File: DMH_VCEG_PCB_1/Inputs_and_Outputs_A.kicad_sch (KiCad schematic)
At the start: 28 parts, among them J1 TS_Jack_6.35mm_Sw, J10 TS_Jack_6.35mm_Sw, J2 TS_Jack_6.35mm_Sw, J200 IDC_02x08, J3 TS_Jack_6.35mm_Sw, J4 TS_Jack_6.35mm_Sw, J5 TS_Jack_6.35mm_Sw, J6 TS_Jack_6.35mm_Sw, J7 TS_Jack_6.35mm_Sw, J8 TS_Jack_6.35mm_Sw, J9 TS_Jack_6.35mm_Sw, U8 TL074, U9 TL074

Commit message: Reanotated schematic
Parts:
- renumbered R1 to R66, R3 to R67, R5 to R68, R6 to R69, R67 to R71, R66 to R72, RV5 to RV15, RV6 to RV16, RV7 to RV17, RV8 to RV18, RV1 to RV19, RV2 to RV20, RV3 to RV21, RV4 to RV22, U9 to U1, U8 to U9
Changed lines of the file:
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@@
 		(dnp no)
 		(fields_autoplaced yes)
-		(property "Reference" "R66"
+		(property "Reference" "R72"
 			(at 165.1 226.06 90)
 			(effects
@@
 			(project "DMH_VCEG_PCB_1"
 				(path "/58f4306d-5387-4983-bb08-41a2313fd315/ce3fef8b-9f1d-4178-b50b-4a046c030679"
-					(reference "R66")
+					(reference "R72")
 					(unit 1)
 				)
@@
 		(on_board yes)
 		(dnp no)
-		(property "Reference" "U9"
+		(property "Reference" "U1"
 			(at 107.95 139.7 0)
 			(effects
@@
 			(project "DMH_VCEG_PCB_1"
 				(path "/58f4306d-5387-4983-bb08-41a2313fd315/ce3fef8b-9f1d-4178-b50b-4a046c030679"
-					(reference "U9")
+					(reference "U1")
 					(unit 4)
 				)
@@
 		(dnp no)
 		(fields_autoplaced yes)
-		(property "Reference" "R6"
+		(property "Reference" "R69"
 			(at 88.9 120.65 90)
 			(effects
@@
 			(project "DMH_VCEG_PCB_1"
 				(path "/58f4306d-5387-4983-bb08-41a2313fd315/ce3fef8b-9f1d-4178-b50b-4a046c030679"
-					(reference "R6")
+					(reference "R69")
 					(unit 1)
 				)
@@
 		(dnp no)
 		(fields_autoplaced yes)
-		(property "Reference" "R5"
+		(property "Reference" "R68"
 			(at 88.9 88.9 90)
 			(effects
@@
 			(project "DMH_VCEG_PCB_1"
 				(path "/58f4306d-5387-4983-bb08-41a2313fd315/ce3fef8b-9f1d-4178-b50b-4a046c030679"
-					(reference "R5")
+					(reference "R68")
 					(unit 1)
 				)
@@
 		(dnp no)
 		(fields_autoplaced yes)
-		(property "Reference" "#PWR03"
+		(property "Reference" "#PWR035"
 			(at 86.36 281.94 0)
 			(effects
@@
 			(project ""
 				(path "/58f4306d-5387-4983-bb08-41a2313fd315/ce3fef8b-9f1d-4178-b50b-4a046c030679"
-					(reference "#PWR03")
+					(reference "#PWR035")
 					(unit 1)
 				)
@@
 		(on_board yes)
 		(dnp no)
-		(property "Reference" "RV3"
+		(property "Reference" "RV21"
 			(at 107.95 88.9 90)
 			(effects
@@
 			(project "DMH_VCEG_PCB_1"
 				(path "/58f4306d-5387-4983-bb08-41a2313fd315/ce3fef8b-9f1d-4178-b50b-4a046c030679"
-					(reference "RV3")
+					(reference "RV21")
 					(unit 1)
 				)
@@
 		(on_board no)
 		(dnp no)
-		(property "Reference" "RV6"
+		(property "Reference" "RV16"
 			(at 73.66 69.8499 0)
 			(effects
@@
 			(project "DMH_VCEG_PCB_1"
 				(path "/58f4306d-5387-4983-bb08-41a2313fd315/ce3fef8b-9f1d-4178-b50b-4a046c030679"
-					(reference "RV6")
+					(reference "RV16")
 					(unit 1)
 				)
@@
 		(on_board yes)
 		(dnp no)
-		(property "Reference" "RV2"
+		(property "Reference" "RV20"
 			(at 107.95 57.15 90)
 			(effects
@@
 			(project "DMH_VCEG_PCB_1"
 				(path "/58f4306d-5387-4983-bb08-41a2313fd315/ce3fef8b-9f1d-4178-b50b-4a046c030679"
-					(reference "RV2")
+					(reference "RV20")
 					(unit 1)
 				)
@@
 				)
 				(hide yes)
+			)
+		)
+		(property "Function" ""
+			(at 63.5 265.43 0)
+			(effects
+				(font
+					(size 1.27 1.27)
+				)
 			)
 		)
@@
 		(on_board yes)
 		(dnp no)
-		(property "Reference" "U9"
+		(property "Reference" "U1"
 			(at 107.95 44.45 0)
 			(effects
@@
 			(project "DMH_VCEG_PCB_1"
 				(path "/58f4306d-5387-4983-bb08-41a2313fd315/ce3fef8b-9f1d-4178-b50b-4a046c030679"
-					(reference "U9")
+					(reference "U1")
 					(unit 1)
 				)
@@
 		(on_board no)
 		(dnp no)
-		(property "Reference" "RV8"
+		(property "Reference" "RV18"
 			(at 73.66 133.3499 0)
 			(effects
@@
 			(project "DMH_VCEG_PCB_1"
 				(path "/58f4306d-5387-4983-bb08-41a2313fd315/ce3fef8b-9f1d-4178-b50b-4a046c030679"
-					(reference "RV8")
+					(reference "RV18")
 					(unit 1)
 				)
@@
 		(on_board yes)
 		(dnp no)
-		(property "Reference" "RV4"
+		(property "Reference" "RV22"
 			(at 107.95 120.65 90)
 			(effects
@@
 			(project "DMH_VCEG_PCB_1"
 				(path "/58f4306d-5387-4983-bb08-41a2313fd315/ce3fef8b-9f1d-4178-b50b-4a046c030679"
-					(reference "RV4")
+					(reference "RV22")
 					(unit 1)
 				)
@@
 		(on_board no)
 		(dnp no)
-		(property "Reference" "RV5"
+		(property "Reference" "RV15"
 			(at 73.66 38.0999 0)
 			(effects
@@
 			(project "DMH_VCEG_PCB_1"
 				(path "/58f4306d-5387-4983-bb08-41a2313fd315/ce3fef8b-9f1d-4178-b50b-4a046c030679"
-					(reference "RV5")
+					(reference "RV15")
 					(unit 1)
 				)
@@
 		(on_board yes)
 		(dnp no)
-		(property "Reference" "U9"
+		(property "Reference" "U1"
 			(at 107.95 76.2 0)
 			(effects
@@
 			(project "DMH_VCEG_PCB_1"
 				(path "/58f4306d-5387-4983-bb08-41a2313fd315/ce3fef8b-9f1d-4178-b50b-4a046c030679"
-					(reference "U9")
+					(reference "U1")
 					(unit 2)
 				)
@@
 		(on_board yes)
 		(dnp no)
-		(property "Reference" "U9"
+		(property "Reference" "U1"
 			(at 107.95 107.95 0)
 			(effects
@@
 			(project "DMH_VCEG_PCB_1"
 				(path "/58f4306d-5387-4983-bb08-41a2313fd315/ce3fef8b-9f1d-4178-b50b-4a046c030679"
-					(reference "U9")
+					(reference "U1")
 					(unit 3)
 				)
@@
 		(dnp no)
 		(fields_autoplaced yes)
-		(property "Reference" "R1"
+		(property "Reference" "R66"
 			(at 88.9 25.4 90)
 			(effects
@@
 			(project "DMH_VCEG_PCB_1"
 				(path "/58f4306d-5387-4983-bb08-41a2313fd315/ce3fef8b-9f1d-4178-b50b-4a046c030679"
-					(reference "R1")
+					(reference "R66")
 					(unit 1)
 				)
@@
 		(dnp no)
 		(fields_autoplaced yes)
-		(property "Reference" "R67"
+		(property "Reference" "R71"
 			(at 146.05 214.63 90)
 			(effects
@@
 			(project "DMH_VCEG_PCB_1"
 				(path "/58f4306d-5387-4983-bb08-41a2313fd315/ce3fef8b-9f1d-4178-b50b-4a046c030679"
-					(reference "R67")
+					(reference "R71")
 					(unit 1)
 				)
@@
 		(dnp no)
 		(fields_autoplaced yes)
-		(property "Reference" "U8"
+		(property "Reference" "U9"
 			(at 146.05 224.79 0)
 			(effects
@@
 			(project ""
 				(path "/58f4306d-5387-4983-bb08-41a2313fd315/ce3fef8b-9f1d-4178-b50b-4a046c030679"
-					(reference "U8")
+					(reference "U9")
 					(unit 4)
 				)
@@
 		(on_board yes)
 		(dnp no)
-		(property "Reference" "RV1"
+		(property "Reference" "RV19"
 			(at 107.95 25.4 90)
 			(effects
@@
 			(project "DMH_VCEG_PCB_1"
 				(path "/58f4306d-5387-4983-bb08-41a2313fd315/ce3fef8b-9f1d-4178-b50b-4a046c030679"
-					(reference "RV1")
+					(reference "RV19")
 					(unit 1)
 				)
@@
 		(on_board no)
 		(dnp no)
-		(property "Reference" "RV7"
+		(property "Reference" "RV17"
 			(at 73.66 101.5999 0)
 			(effects
@@
 			(project "DMH_VCEG_PCB_1"
 				(path "/58f4306d-5387-4983-bb08-41a2313fd315/ce3fef8b-9f1d-4178-b50b-4a046c030679"
-					(reference "RV7")
+					(reference "RV17")
 					(unit 1)
 				)
@@
 		(dnp no)
 		(fields_autoplaced yes)
-		(property "Reference" "R3"
+		(property "Reference" "R67"
 			(at 88.9 57.15 90)
 			(effects
@@
 			(project "DMH_VCEG_PCB_1"
 				(path "/58f4306d-5387-4983-bb08-41a2313fd315/ce3fef8b-9f1d-4178-b50b-4a046c030679"
-					(reference "R3")
-					(unit 1)
-				)
+					(reference "R67")
+					(unit 1)
+				)

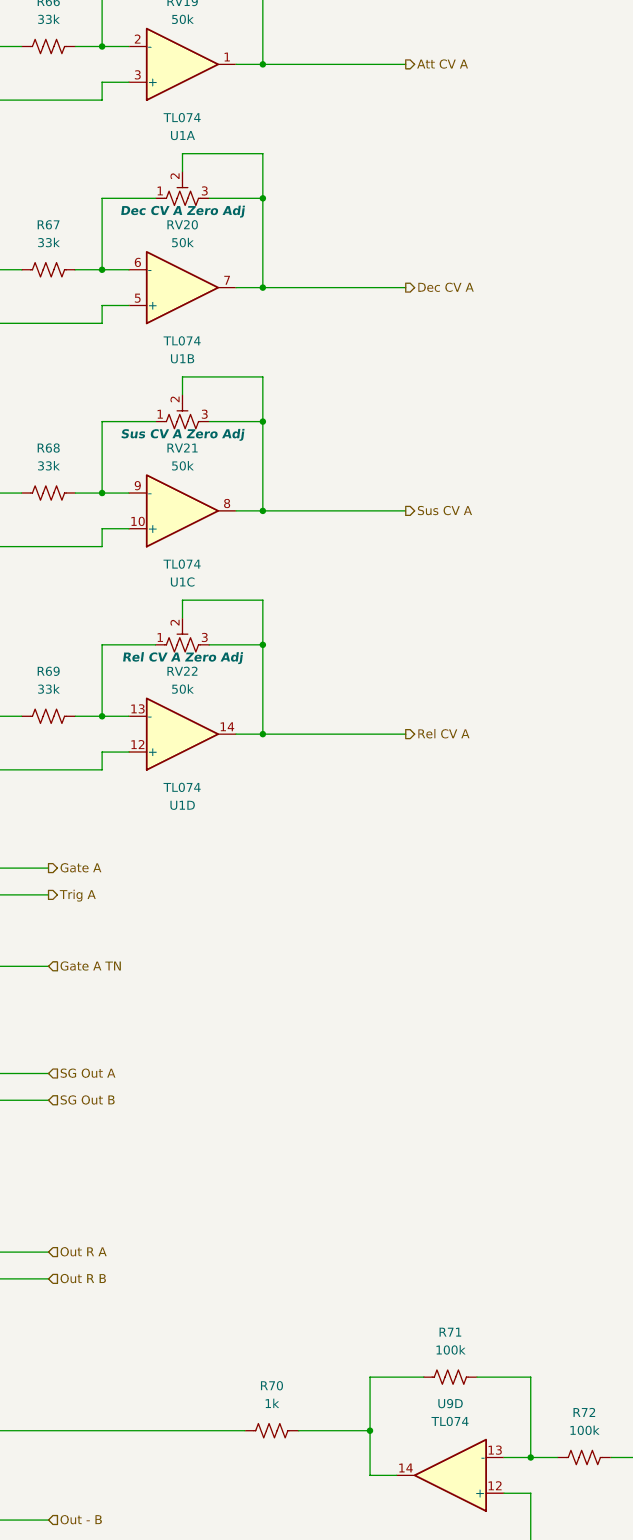
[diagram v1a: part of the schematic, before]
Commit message: Reannotated ICs to match MFOS schematic
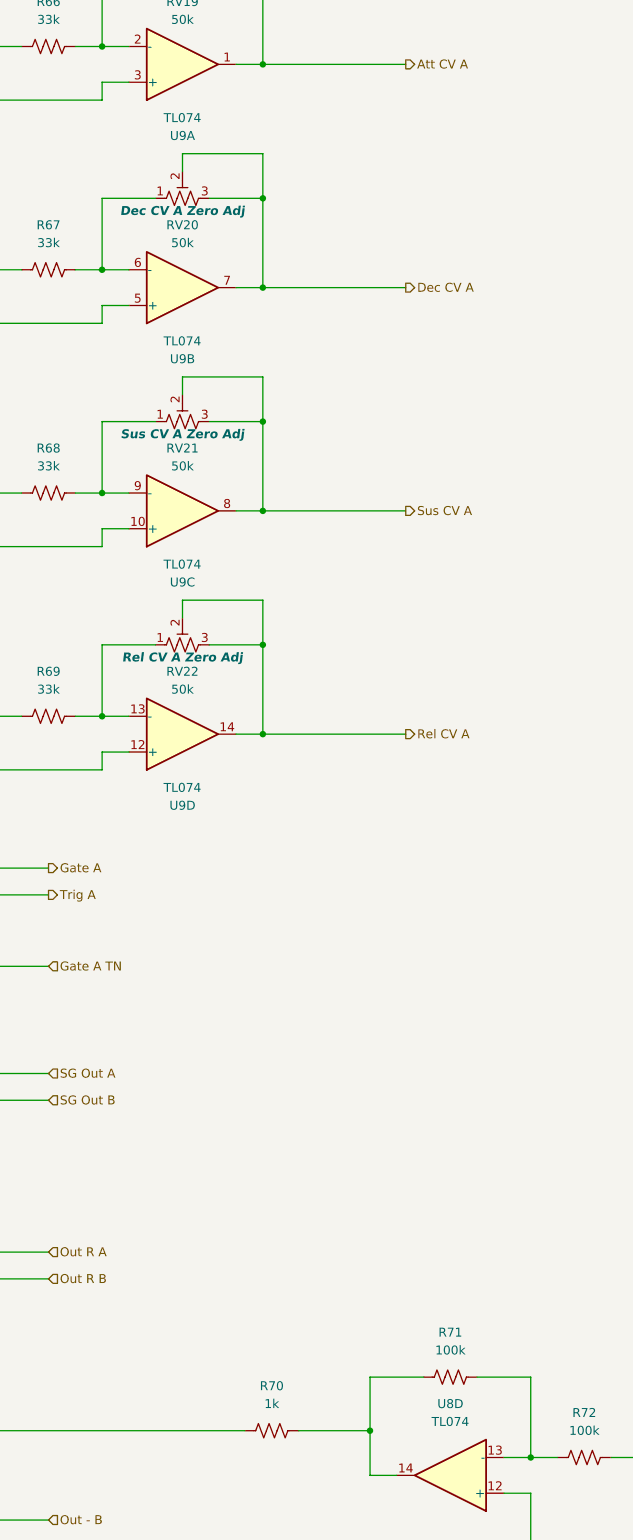
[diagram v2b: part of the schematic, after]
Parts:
- renumbered U9 to U8, U1 to U9
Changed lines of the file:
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@@
 		(on_board yes)
 		(dnp no)
-		(property "Reference" "U1"
+		(property "Reference" "U9"
 			(at 107.95 139.7 0)
 			(effects
@@
 			(project "DMH_VCEG_PCB_1"
 				(path "/58f4306d-5387-4983-bb08-41a2313fd315/ce3fef8b-9f1d-4178-b50b-4a046c030679"
-					(reference "U1")
+					(reference "U9")
 					(unit 4)
 				)
@@
 		(on_board yes)
 		(dnp no)
-		(property "Reference" "U1"
+		(property "Reference" "U9"
 			(at 107.95 44.45 0)
 			(effects
@@
 			(project "DMH_VCEG_PCB_1"
 				(path "/58f4306d-5387-4983-bb08-41a2313fd315/ce3fef8b-9f1d-4178-b50b-4a046c030679"
-					(reference "U1")
+					(reference "U9")
 					(unit 1)
 				)
@@
 		(on_board yes)
 		(dnp no)
-		(property "Reference" "U1"
+		(property "Reference" "U9"
 			(at 107.95 76.2 0)
 			(effects
@@
 			(project "DMH_VCEG_PCB_1"
 				(path "/58f4306d-5387-4983-bb08-41a2313fd315/ce3fef8b-9f1d-4178-b50b-4a046c030679"
-					(reference "U1")
+					(reference "U9")
 					(unit 2)
 				)
@@
 		(on_board yes)
 		(dnp no)
-		(property "Reference" "U1"
+		(property "Reference" "U9"
 			(at 107.95 107.95 0)
 			(effects
@@
 			(project "DMH_VCEG_PCB_1"
 				(path "/58f4306d-5387-4983-bb08-41a2313fd315/ce3fef8b-9f1d-4178-b50b-4a046c030679"
-					(reference "U1")
+					(reference "U9")
 					(unit 3)
 				)
@@
 		(dnp no)
 		(fields_autoplaced yes)
-		(property "Reference" "U9"
+		(property "Reference" "U8"
 			(at 146.05 224.79 0)
 			(effects
@@
 			(project ""
 				(path "/58f4306d-5387-4983-bb08-41a2313fd315/ce3fef8b-9f1d-4178-b50b-4a046c030679"
-					(reference "U9")
+					(reference "U8")
 					(unit 4)
 				)

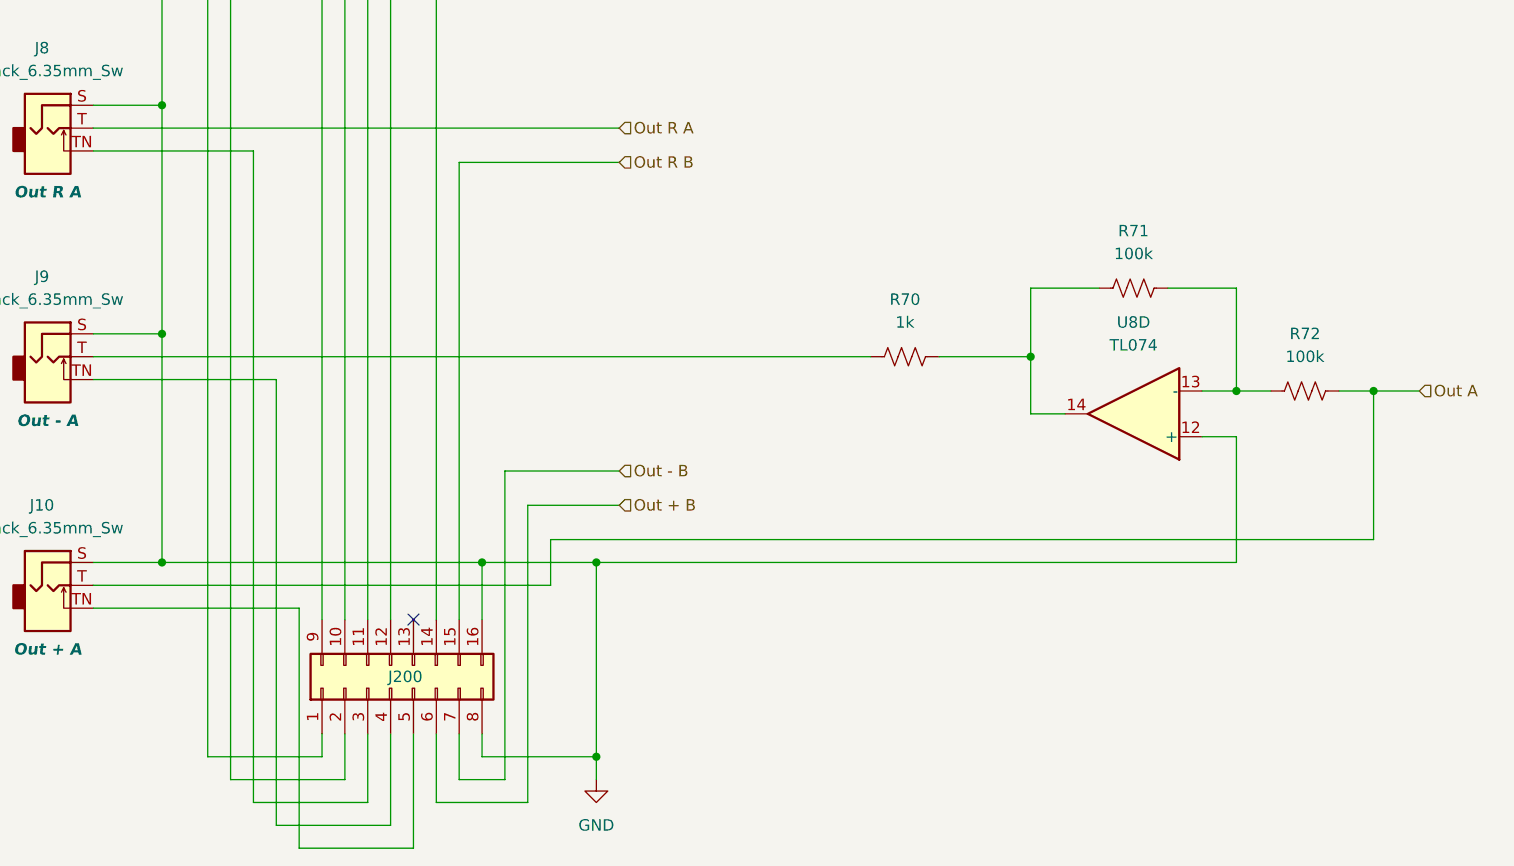
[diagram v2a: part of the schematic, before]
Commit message: Fixed inverted Out and some fp assignments
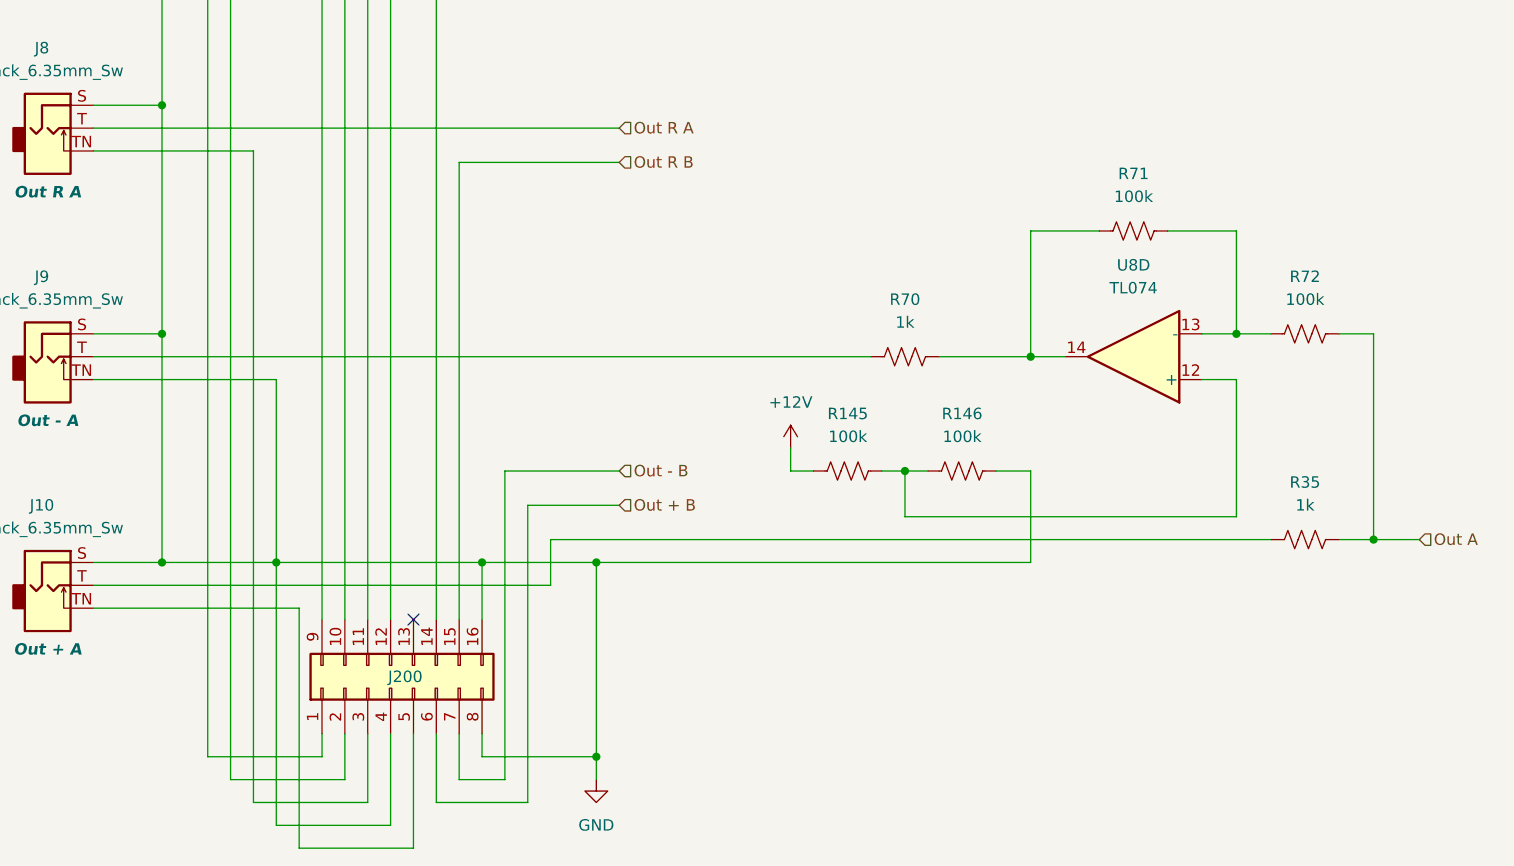
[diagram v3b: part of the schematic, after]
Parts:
- added R145, R146: 100k, Resistor_THT:R_Axial_DIN0207_L6.3mm_D2.5mm_P7.62mm_Horizontal, symbol Device:R_US
- added R35: 1k, Resistor_THT:R_Axial_DIN0207_L6.3mm_D2.5mm_P7.62mm_Horizontal, symbol Device:R_US
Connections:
- net GND: now also J200.4 (Pin_4), J9.TN, R146.1; no longer U8.12 (+)
- net Out A: now also R35.1; no longer J10.T
- new net: J10.T, R35.2
- new net: R145.1, R146.2, U8.12 (+)
- new net +12V: R145.2
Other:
- moved on the sheet: R71, R72, U8D

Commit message: PCB 1 ready for placement
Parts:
- removed U8: TL074, Package_DIP:DIP-14_W7.62mm_Socket, symbol Amplifier_Operational:TL074
- added J21, J22, J23: Conn_01x10_PinHeader, Connector_PinHeader_2.54mm:PinHeader_1x10_P2.54mm_Vertical, symbol SynthStuff:Conn_01x10_PinHeader
- added J27: Conn_01x06_PinHeader, Connector_PinHeader_2.54mm:PinHeader_1x06_P2.54mm_Vertical, symbol SynthStuff:Conn_01x06_PinHeader
- added U21: TL072, Package_DIP:DIP-8_W7.62mm, symbol Amplifier_Operational:TL072
- RV19, RV20, RV21, RV22: footprint Potentiometer_THT:Potentiometer_Bourns_3296W_Vertical -> Potentiometer_THT:Potentiometer_Bourns_3296X_Horizontal
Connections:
- net +12V: now also J21.1 (Pin_1)
- net Att CV A: now also J21.3 (Pin_3)
- net Dec CV A: now also J21.6 (Pin_6)
- net GND: now also J21.2 (Pin_2), J22.2 (Pin_2), J23.1 (Pin_1), J23.2 (Pin_2), J27.3 (Pin_3), J27.4 (Pin_4)
- net Out A: now also J27.2 (Pin_2)
- net Rel CV A: now also J21.10 (Pin_10)
- net Sus CV A: now also J21.7 (Pin_7)
- net at R71.1, R72.2: now also U21.2 (-)
- net at J4.T, R69.1, RV18.3: now also J21.9 (Pin_9)
- net at J3.T, R68.1, RV17.3: now also J21.8 (Pin_8)
- net at J2.T, R67.1, RV16.3: now also J21.5 (Pin_5)
- net at J1.T, R66.1, RV15.3: now also J21.4 (Pin_4)
- net at R70.1, R71.2: now also U21.1
- net at J9.T, R70.2: now also J27.1 (Pin_1)
- net at R145.1, R146.2: now also U21.3 (+)
- new net -12V: J22.1 (Pin_1)
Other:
- note added: "PCB 2"
- moved on the sheet: R35, R66, R67, R68, R69, RV15, RV16, RV17, RV18, RV19, RV20, RV21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

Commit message: Placed ICs and pin headers on PCB 2
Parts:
- U21: footprint Package_DIP:DIP-8_W7.62mm -> Package_DIP:DIP-8_W7.62mm_Socket
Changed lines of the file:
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@@
 			)
 		)
-		(property "Footprint" "Package_DIP:DIP-8_W7.62mm"
+		(property "Footprint" "Package_DIP:DIP-8_W7.62mm_Socket"
 			(at 146.05 228.6 0)
 			(effects
